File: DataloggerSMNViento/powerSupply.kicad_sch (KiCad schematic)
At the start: 11 parts, among them J2 Screw_Terminal_01x02, J3 Vcc 5V StepDown, J4 GND StepDowm, U3 LM2596S-HW-319-v6_module, U5 LM358

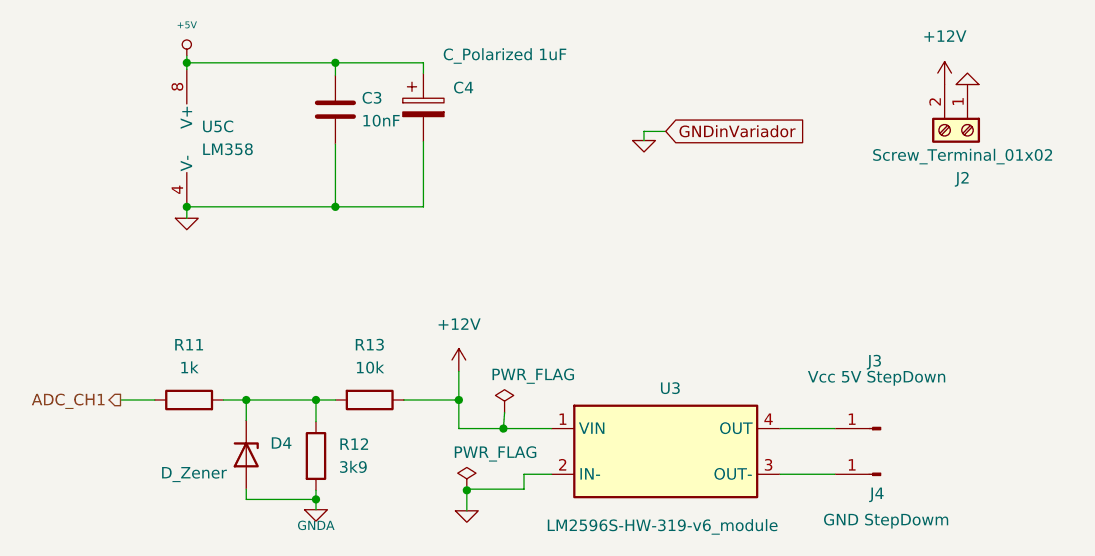
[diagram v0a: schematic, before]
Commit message: Se cambio la alimentacion de los modulos por el stepDown
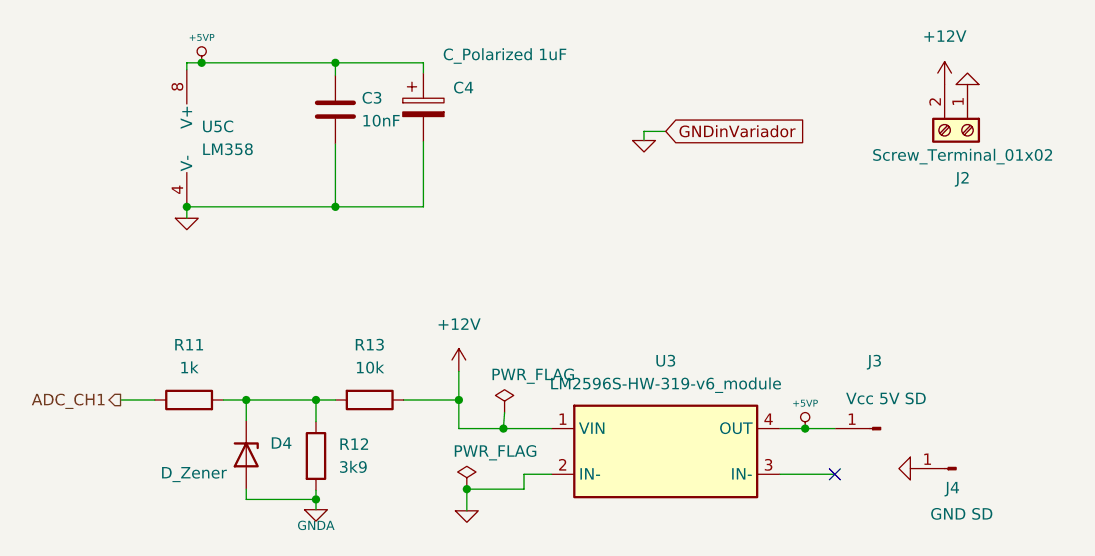
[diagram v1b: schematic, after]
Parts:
- D4: footprint Diode_SMD:D_1812_4532Metric -> Diode_THT:D_DO-34_SOD68_P7.62mm_Horizontal
- J3: value Vcc 5V StepDown -> Vcc 5V SD
- J4: value GND StepDowm -> GND SD
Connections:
- net +5V is gone; now on net +5VP: C3.1, C4.1, U5.8 (V+)
- net GND: now also J4.1 (Pin_1)
- net at U3.3 (IN-): no longer J4.1 (Pin_1)
- net +5VP: now reaches J3.1 (Pin_1), U3.4 (OUT)
- no-connect marks 0 -> 1
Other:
- moved on the sheet: J4

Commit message: Se debe cambiar el diseño porque el footprint del  StepDown esta invertido, lo cual va a implicar cambiar algunas pistas
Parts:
- C4: footprint Capacitor_SMD:CP_Elec_6.3x9.9 -> Capacitor_SMD:CP_Elec_4x5.3
- U5: footprint Package_SO:SO-8_3.9x4.9mm_P1.27mm -> Package_SO:SOIC-8_3.9x4.9mm_P1.27mm
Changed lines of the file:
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@@
       (effects (font (size 1.27 1.27)) (justify left))
     )
-    (property "Footprint" "Package_SO:SO-8_3.9x4.9mm_P1.27mm" (id 2) (at 82.169 46.863 0)
+    (property "Footprint" "Package_SO:SOIC-8_3.9x4.9mm_P1.27mm" (id 2) (at 82.169 46.863 0)
       (effects (font (size 1.27 1.27)) hide)
     )
@@
       (effects (font (size 1.27 1.27)) (justify left))
     )
-    (property "Footprint" "Capacitor_SMD:CP_Elec_6.3x9.9" (id 2) (at 106.8832 47.244 0)
+    (property "Footprint" "Capacitor_SMD:CP_Elec_4x5.3" (id 2) (at 106.8832 47.244 0)
       (effects (font (size 1.27 1.27)) hide)
     )
